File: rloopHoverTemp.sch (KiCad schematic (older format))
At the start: 24 parts, among them P1 CONN_01X02, P2 CONN_01X02, Q1 Q_NPN_BEC, Q2 Q_NPN_BEC, U1 XTR117, U2 TS305-10C50, U3 LTC2054, U4 XTR117, U5 LTC2054

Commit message: prelim layout
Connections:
- net 24V_A: now reaches C2.2, C3.1, P1.1 (P1), Q1.3 (C), U1.7 (V+)
- net 24V_B: now reaches C5.2, C6.1, P2.1 (P1), Q2.3 (C), U4.7 (V+)
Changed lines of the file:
@@
 NoConn ~ 4200 4750
 NoConn ~ 5000 4750
+Text Label 7900 1450 0    39   ~ 0
+24V_A
+Text Label 7900 4050 0    39   ~ 0
+24V_B
 $EndSCHEMATC

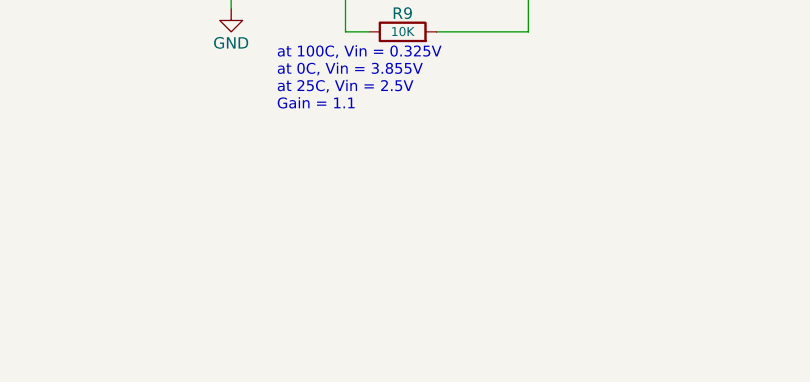
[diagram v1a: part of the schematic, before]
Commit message: more spacing for 24V, better route, gnd'd mnts
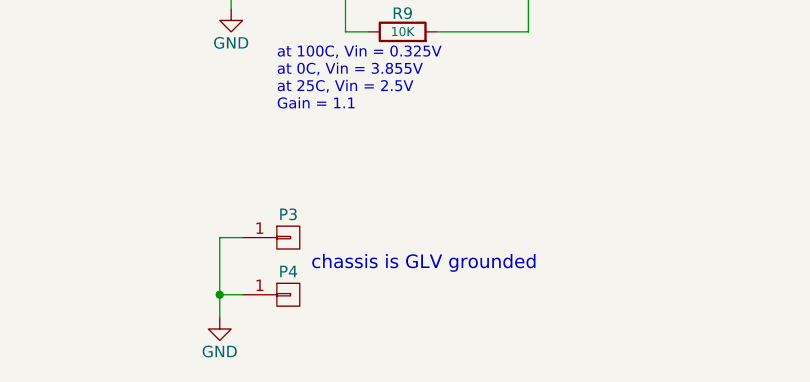
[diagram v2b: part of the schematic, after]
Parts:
- added P3, P4: CONN_01X01, -footprints:SCREWPAD-4-40, symbol CONN_01X01
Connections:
- net GND: now also P3.1 (P1), P4.1 (P1)
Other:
- note added: "chassis is GLV grounded"
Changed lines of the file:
@@
 LIBS:valves
 LIBS:rloop
+LIBS:rloopHoverTemp-cache
 EELAYER 25 0
 EELAYER END
@@
 Text Label 7900 4050 0    39   ~ 0
 24V_B
+$Comp
+L CONN_01X01 P3
+U 1 1 573AB7DF
+P 3950 5850
+F 0 "P3" H 3950 5950 50  0000 C CNN
+F 1 "CONN_01X01" V 4050 5850 50  0001 C CNN
+F 2 "-footprints:SCREWPAD-4-40" H 3950 5850 50  0001 C CNN
+F 3 "" H 3950 5850 50  0000 C CNN
+	1    3950 5850
+	1    0    0    -1
+$EndComp
+$Comp
+L CONN_01X01 P4
+U 1 1 573ABD3A
+P 3950 6100
+F 0 "P4" H 3950 6200 50  0000 C CNN
+F 1 "CONN_01X01" V 4050 6100 50  0001 C CNN
+F 2 "-footprints:SCREWPAD-4-40" H 3950 6100 50  0001 C CNN
+F 3 "" H 3950 6100 50  0000 C CNN
+	1    3950 6100
+	1    0    0    -1
+$EndComp
+$Comp
+L GND #PWR08
+U 1 1 573ABDA2
+P 3650 6200
+F 0 "#PWR08" H 3650 5950 50  0001 C CNN
+F 1 "GND" H 3650 6050 50  0000 C CNN
+F 2 "" H 3650 6200 50  0000 C CNN
+F 3 "" H 3650 6200 50  0000 C CNN
+	1    3650 6200
+	1    0    0    -1
+$EndComp
+Wire Wire Line
+	3750 5850 3650 5850
+Wire Wire Line
+	3650 5850 3650 6200
+Wire Wire Line
+	3750 6100 3650 6100
+Connection ~ 3650 6100
+Text Notes 4050 6000 0    59   ~ 0
+chassis is GLV grounded
 $EndSCHEMATC

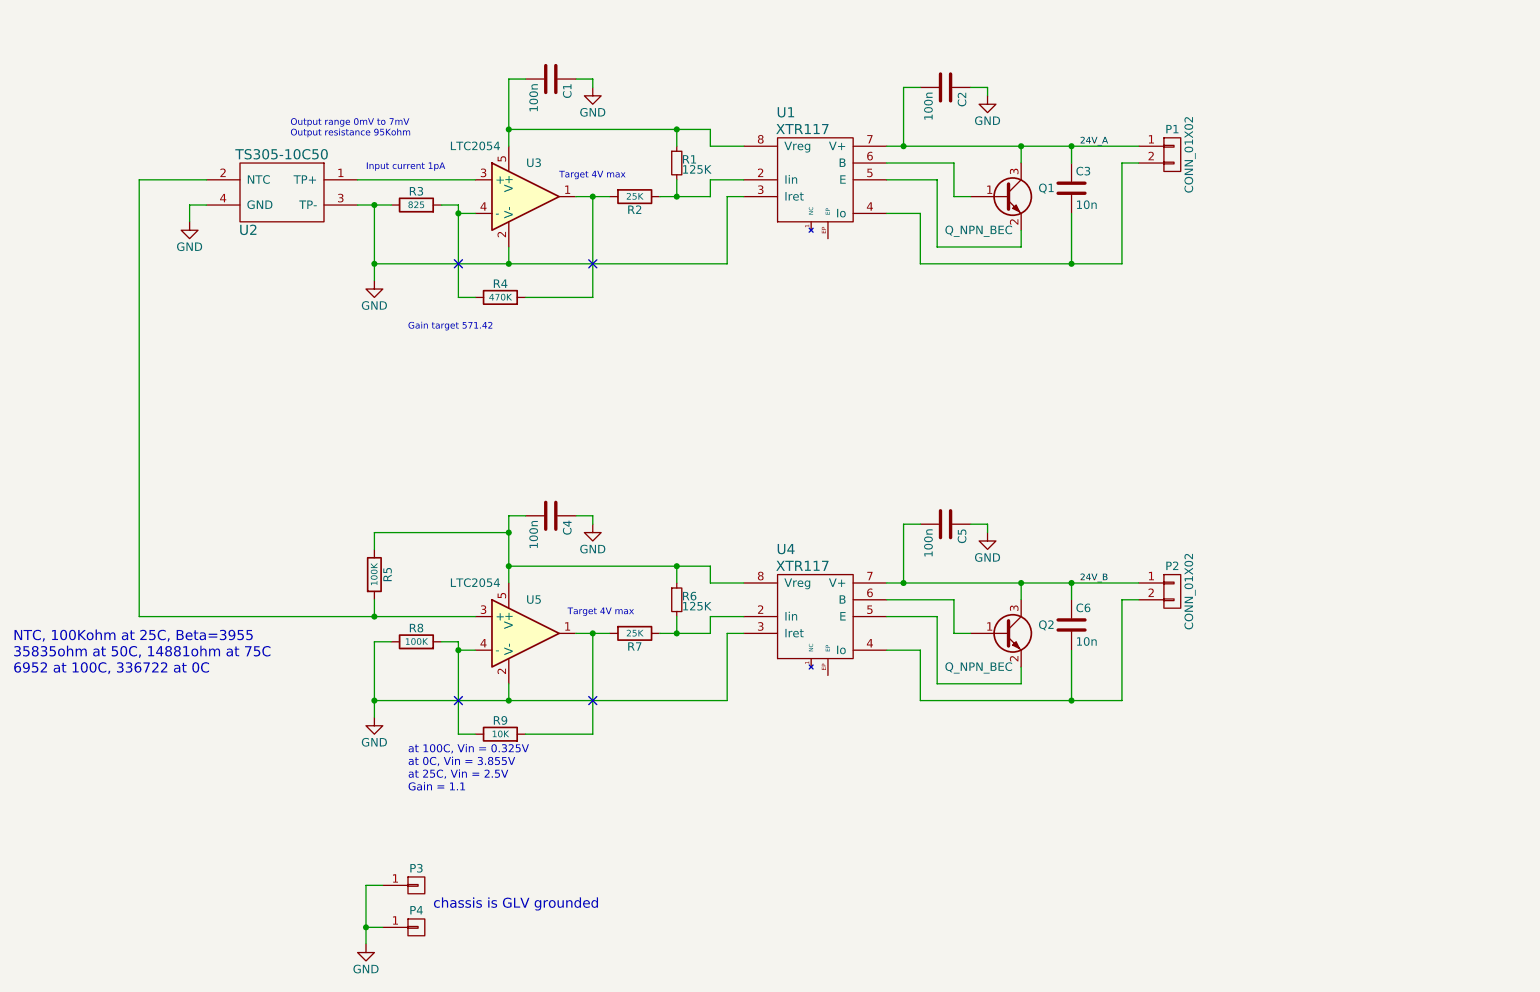
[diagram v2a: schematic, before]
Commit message: split the grounds
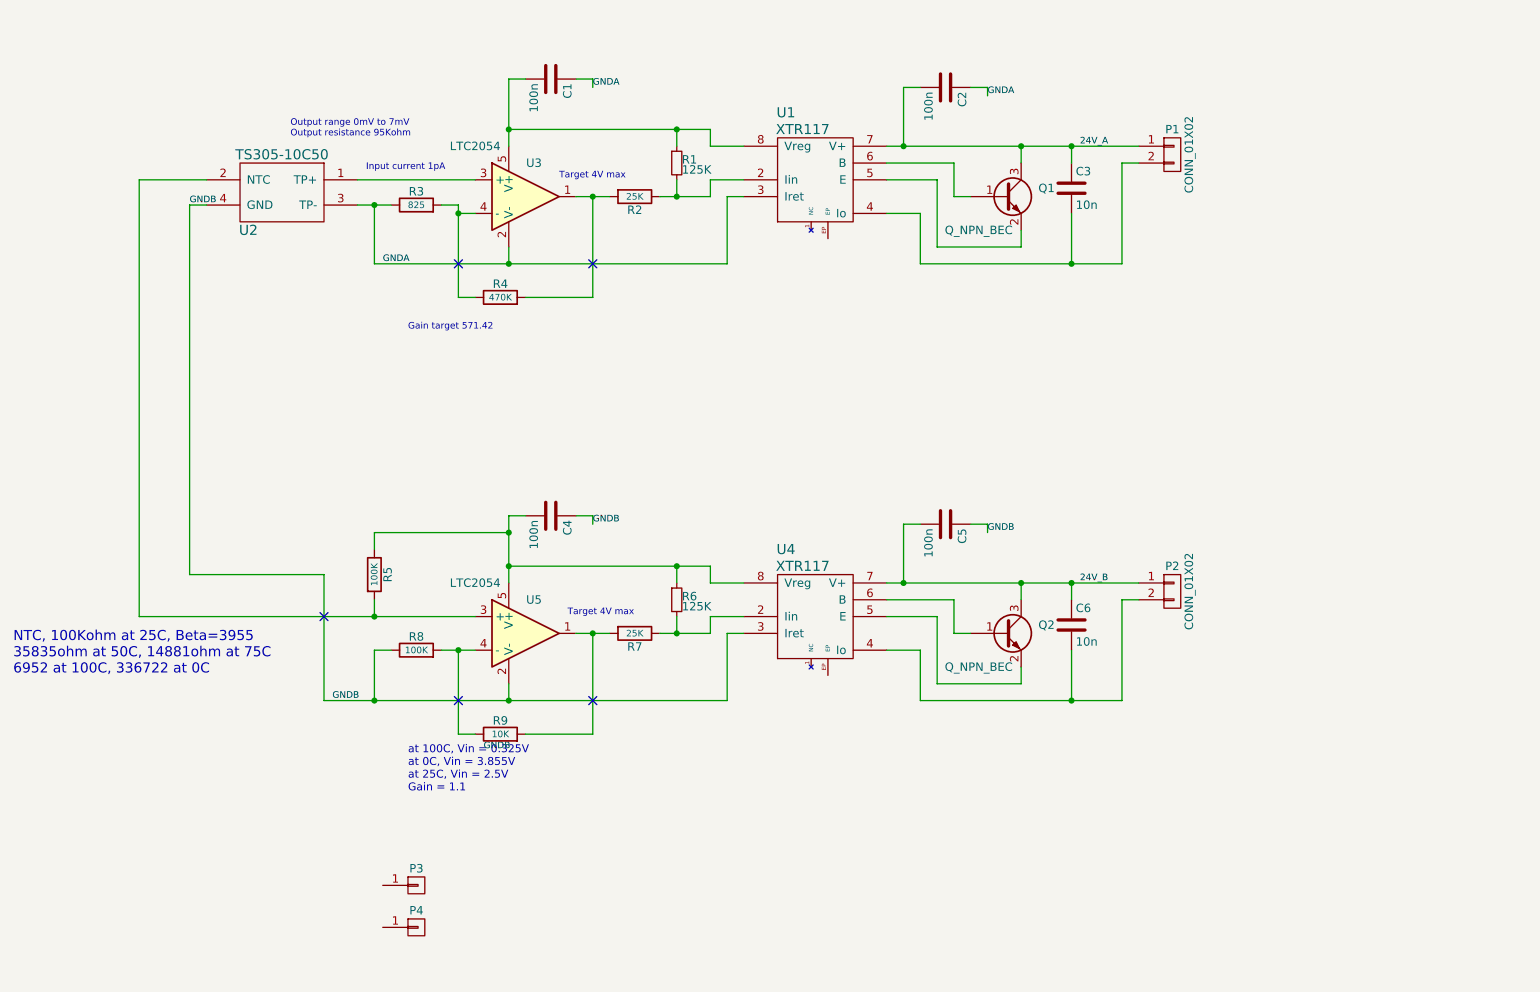
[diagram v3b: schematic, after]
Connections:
- removed net GND: C1.1, C2.1, C4.1, C5.1, P3.1 (P1), P4.1 (P1), R3.1, R8.1, U1.3 (Iret), U2.3 (TP-), U2.4 (GND), U3.2 (V-), U4.3 (Iret), U5.2 (V-)
- new net GNDA: C1.1, C2.1, R3.1, U1.3 (Iret), U2.3 (TP-), U3.2 (V-)
- new net GNDB: C4.1, C5.1, R8.1, U2.4 (GND), U4.3 (Iret), U5.2 (V-)
- no-connect marks 4 -> 5
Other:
- note removed: "chassis is GLV grounded"
- moved on the sheet: R8
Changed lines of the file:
@@
-$EndComp
-$Comp
-L GND #PWR01
-U 1 1 573AAD0F
-P 3700 2250
-F 0 "#PWR01" H 3700 2000 50  0001 C CNN
-F 1 "GND" H 3700 2100 50  0000 C CNN
-F 2 "" H 3700 2250 50  0000 C CNN
-F 3 "" H 3700 2250 50  0000 C CNN
-	1    3700 2250
-	1    0    0    -1
-$EndComp
-$Comp
-L GND #PWR02
-U 1 1 573AAE35
-P 5000 1100
-F 0 "#PWR02" H 5000 850 50  0001 C CNN
-F 1 "GND" H 5000 950 50  0000 C CNN
-F 2 "" H 5000 1100 50  0000 C CNN
-F 3 "" H 5000 1100 50  0000 C CNN
-	1    5000 1100
-	1    0    0    -1
-$EndComp
-$Comp
-L GND #PWR03
-U 1 1 573AAE64
-P 7350 1150
-F 0 "#PWR03" H 7350 900 50  0001 C CNN
-F 1 "GND" H 7350 1000 50  0000 C CNN
-F 2 "" H 7350 1150 50  0000 C CNN
-F 3 "" H 7350 1150 50  0000 C CNN
-	1    7350 1150
-	1    0    0    -1
-$EndComp
-$Comp
-L GND #PWR04
-U 1 1 573AC1F1
-P 2600 1900
-F 0 "#PWR04" H 2600 1650 50  0001 C CNN
-F 1 "GND" H 2600 1750 50  0000 C CNN
-F 2 "" H 2600 1900 50  0000 C CNN
-F 3 "" H 2600 1900 50  0000 C CNN
-	1    2600 1900
-	1    0    0    -1
 $EndComp
 $Comp
@@
 L R R8
 U 1 1 573AC522
-P 3950 4400
-F 0 "R8" V 4030 4400 50  0000 C CNN
-F 1 "100K" V 3950 4400 39  0000 C CNN
-F 2 "Resistors_SMD:R_0603_HandSoldering" V 3880 4400 50  0001 C CNN
-F 3 "" H 3950 4400 50  0000 C CNN
-	1    3950 4400
+P 3950 4450
+F 0 "R8" V 4030 4450 50  0000 C CNN
+F 1 "100K" V 3950 4450 39  0000 C CNN
+F 2 "Resistors_SMD:R_0603_HandSoldering" V 3880 4450 50  0001 C CNN
+F 3 "" H 3950 4450 50  0000 C CNN
+	1    3950 4450
 	0    -1   -1   0
 $EndComp
@@
 $EndComp
 $Comp
-L GND #PWR05
-U 1 1 573AC53A
-P 3700 4850
-F 0 "#PWR05" H 3700 4600 50  0001 C CNN
-F 1 "GND" H 3700 4700 50  0000 C CNN
-F 2 "" H 3700 4850 50  0000 C CNN
-F 3 "" H 3700 4850 50  0000 C CNN
-	1    3700 4850
-	1    0    0    -1
-$EndComp
-$Comp
-L GND #PWR06
-U 1 1 573AC540
-P 5000 3700
-F 0 "#PWR06" H 5000 3450 50  0001 C CNN
-F 1 "GND" H 5000 3550 50  0000 C CNN
-F 2 "" H 5000 3700 50  0000 C CNN
-F 3 "" H 5000 3700 50  0000 C CNN
-	1    5000 3700
-	1    0    0    -1
-$EndComp
-$Comp
-L GND #PWR07
-U 1 1 573AC546
-P 7350 3750
-F 0 "#PWR07" H 7350 3500 50  0001 C CNN
-F 1 "GND" H 7350 3600 50  0000 C CNN
-F 2 "" H 7350 3750 50  0000 C CNN
-F 3 "" H 7350 3750 50  0000 C CNN
-	1    7350 3750
-	1    0    0    -1
-$EndComp
-$Comp
 L R R5
 U 1 1 573AD72C
@@
 	5900 1450 5700 1450
 Wire Wire Line
-	5700 1450 5700 1350
-Wire Wire Line
-	5700 1350 4500 1350
+	5700 1350 5700 1450
+Wire Wire Line
+	4500 1350 5700 1350
 Wire Wire Line
 	4500 1050 4500 1450
@@
 	8250 1550 8150 1550
 Wire Wire Line
-	8150 1550 8150 2150
-Wire Wire Line
-	8150 2150 6950 2150
+	8150 2150 8150 1550
+Wire Wire Line
+	6950 2150 8150 2150
 Wire Wire Line
 	6950 2150 6950 1850
@@
 	3600 1800 3800 1800
 Wire Wire Line
-	3700 1800 3700 2250
+	3700 1800 3700 2150
 Connection ~ 4500 2150
 Connection ~ 3700 1800
@@
 	4200 1850 4300 1850
 Connection ~ 4200 1850
-Connection ~ 3700 2150
 Wire Wire Line
 	4900 1050 5000 1050
@@
 	2700 1800 2600 1800
 Wire Wire Line
-	2600 1800 2600 1900
+	2600 1800 2600 4000
 Wire Wire Line
 	5900 4050 5700 4050
 Wire Wire Line
-	5700 4050 5700 3950
-Wire Wire Line
-	5700 3950 4500 3950
+	5700 3950 5700 4050
+Wire Wire Line
+	4500 3950 5700 3950
 Wire Wire Line
 	4500 3650 4500 4050
@@
 Connection ~ 5500 4350
 Wire Wire Line
-	4500 4650 4500 4750
-Wire Wire Line
-	3700 4750 5800 4750
+	4500 4750 4500 4650
+Wire Wire Line
+	3400 4750 5800 4750
 Wire Wire Line
 	5800 4750 5800 4350
@@
 	8250 4150 8150 4150
 Wire Wire Line
-	8150 4150 8150 4750
-Wire Wire Line
-	8150 4750 6950 4750
+	8150 4750 8150 4150
+Wire Wire Line
+	6950 4750 8150 4750
 Wire Wire Line
 	6950 4750 6950 4450
@@
 Wire Wire Line
 	2300 4250 4300 4250
-Wire Wire Line
-	3700 4400 3700 4850
 Connection ~ 4500 4750
 Wire Wire Line
@@
 Connection ~ 4500 3750
 Wire Wire Line
-	4200 4400 4200 4950
+	4100 4450 4300 4450
+Wire Wire Line
+	4200 4450 4200 4950
 Connection ~ 4200 4450
 Wire Wire Line
-	4200 4450 4300 4450
-Wire Wire Line
-	3800 4400 3700 4400
-Wire Wire Line
-	4200 4400 4100 4400
+	3800 4450 3700 4450
 Text Notes 4800 1650 0    39   ~ 0
 Target 4V max
@@
 	1    0    0    -1
 $EndComp
-$Comp
-L GND #PWR08
-U 1 1 573ABDA2
-P 3650 6200
-F 0 "#PWR08" H 3650 5950 50  0001 C CNN
-F 1 "GND" H 3650 6050 50  0000 C CNN
-F 2 "" H 3650 6200 50  0000 C CNN
-F 3 "" H 3650 6200 50  0000 C CNN
-	1    3650 6200
-	1    0    0    -1
-$EndComp
-Wire Wire Line
-	3750 5850 3650 5850
-Wire Wire Line
-	3650 5850 3650 6200
-Wire Wire Line
-	3750 6100 3650 6100
-Connection ~ 3650 6100
-Text Notes 4050 6000 0    59   ~ 0
-chassis is GLV grounded
+Text Label 4350 5050 0    39   ~ 0
+GNDB
+Text Label 2600 1800 0    39   ~ 0
+GNDB
+Text Label 3750 2150 0    39   ~ 0
+GNDA
+Wire Wire Line
+	3700 4450 3700 4750
+Wire Wire Line
+	3400 4750 3400 4000
+Wire Wire Line
+	3400 4000 2600 4000
+NoConn ~ 3400 4250
+Text Label 5000 1100 0    39   ~ 0
+GNDA
+Text Label 7350 1150 0    39   ~ 0
+GNDA
+Text Label 7350 3750 0    39   ~ 0
+GNDB
+Text Label 5000 3700 0    39   ~ 0
+GNDB
+Text Label 3450 4750 0    39   ~ 0
+GNDB
 $EndSCHEMATC
